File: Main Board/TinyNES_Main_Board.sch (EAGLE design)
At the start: 118 parts, among them J1 VIDEO, J2 AUDIO, J3 TRRS, J4 USB-C, P1 100k, Q1 3906, U1 BUFFER, U10 74X1G74, U11 74X1G74, U12 NCS603, U13 74X373, U14 CPU, U15 74X139, U16 PPU, U17 74X240, U18 BUFFER, U19 APX811, U2 SIT2001B, U20 FPF210X, U21 NOR, U22 XOR, U3 ICS501, U4 BUFFER, U5 2KB, U6 2KB, U7 PL133-37, U8 SIT2001B, U9 AP2138N

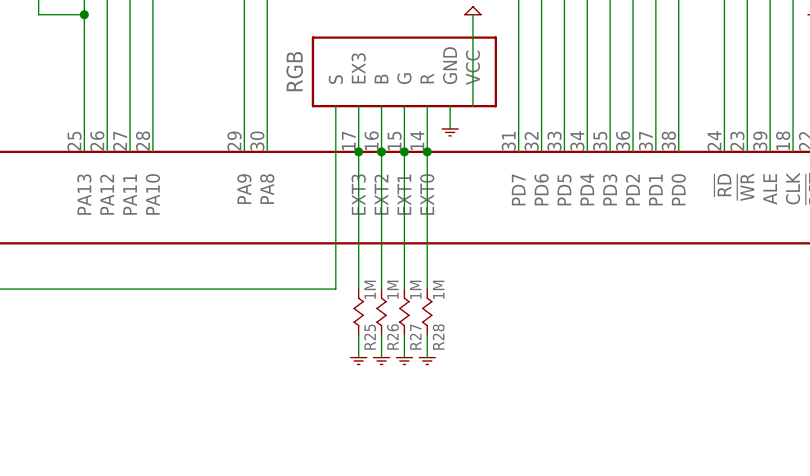
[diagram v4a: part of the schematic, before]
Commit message: minor resistor component value change
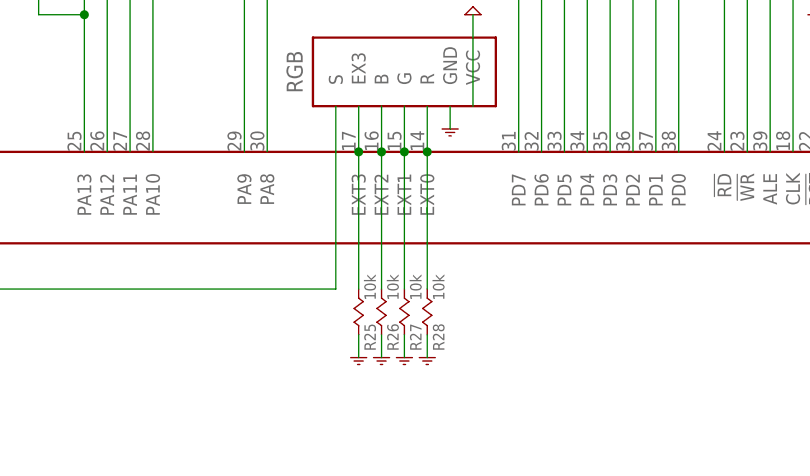
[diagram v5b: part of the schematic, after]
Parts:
- R25, R26, R27, R28: value 1M -> 10k
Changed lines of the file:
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@@
 <part name="GND38" library="TinyNES_Library" deviceset="GND" device=""/>
 <part name="GND39" library="TinyNES_Library" deviceset="GND" device=""/>
-<part name="R28" library="TinyNES_Library" deviceset="RESISTOR" device="-0603" value="1M"/>
-<part name="R27" library="TinyNES_Library" deviceset="RESISTOR" device="-0603" value="1M"/>
-<part name="R26" library="TinyNES_Library" deviceset="RESISTOR" device="-0603" value="1M"/>
-<part name="R25" library="TinyNES_Library" deviceset="RESISTOR" device="-0603" value="1M"/>
+<part name="R28" library="TinyNES_Library" deviceset="RESISTOR" device="-0603" value="10k"/>
+<part name="R27" library="TinyNES_Library" deviceset="RESISTOR" device="-0603" value="10k"/>
+<part name="R26" library="TinyNES_Library" deviceset="RESISTOR" device="-0603" value="10k"/>
+<part name="R25" library="TinyNES_Library" deviceset="RESISTOR" device="-0603" value="10k"/>
 <part name="GND13" library="TinyNES_Library" deviceset="GND" device=""/>
 <part name="GND40" library="TinyNES_Library" deviceset="GND" device=""/>
